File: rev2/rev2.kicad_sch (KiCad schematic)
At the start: 32 parts, among them J1 Termination, J2 CAN1, J3 Termination, J4 CAN2, J5 SWD ASYNC, J6 LIN Pots, J7 AIN, SW1 SW_Push, SW2 SW_SPDT, U1 STM32F429ZITx, U2 TJA1051T, U3 TJA1051T, U5 AMS1117-3.3, Y3 16MHz

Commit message: got the pcb into size constraint now need to try and see if routing is possible
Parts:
- added C30, C31, C32, C33, C38, C39, C40, C41, C42, C43, C44, C45, C46, C48: 100n, Capacitor_SMD:C_0603_1608Metric_Pad1.08x0.95mm_HandSolder, symbol Device:C
- added C47: 4.7u, Capacitor_SMD:C_0603_1608Metric_Pad1.08x0.95mm_HandSolder, symbol Device:C
- added C49: 1u, Capacitor_SMD:C_0603_1608Metric_Pad1.08x0.95mm_HandSolder, symbol Device:C
- added J10: GPIO, TerminalBlock_Phoenix:TerminalBlock_Phoenix_MPT-0,5-8-2.54_1x08_P2.54mm_Horizontal, symbol Connector:Screw_Terminal_01x08
- added J8: USB_OTG, Connector_USB:USB_Mini-B_Wuerth_65100516121_Horizontal, symbol Connector:USB_OTG
- added J9: PWR_USB, Connector_USB:USB_C_Receptacle_GCT_USB4105-xx-A_16P_TopMnt_Horizontal, symbol Connector:USB_C_Receptacle_PowerOnly_6P
- added U6: ~, Package_TO_SOT_SMD:SOT-23-5_HandSoldering, symbol custom parts library:STMPS2151STR
- C21, C22, C23, C24, C25, C28, C29: footprint (none) -> Capacitor_SMD:C_0603_1608Metric_Pad1.08x0.95mm_HandSolder
- C26: renamed from C24; footprint Capacitor_SMD:C_0603_1608Metric -> Capacitor_SMD:C_0603_1608Metric_Pad1.08x0.95mm_HandSolder
- C27: renamed from C25; footprint Capacitor_SMD:C_0603_1608Metric -> Capacitor_SMD:C_0603_1608Metric_Pad1.08x0.95mm_HandSolder
- J1, J3: footprint (none) -> Connector_PinHeader_2.54mm:PinHeader_1x02_P2.54mm_Vertical
- J2, J4: footprint (none) -> TerminalBlock_Phoenix:TerminalBlock_Phoenix_MPT-0,5-2-2.54_1x02_P2.54mm_Horizontal
- J5: footprint (none) -> Connector_PinHeader_2.54mm:PinHeader_2x05_P2.54mm_Vertical
- J6, J7: footprint (none) -> TerminalBlock_Phoenix:TerminalBlock_Phoenix_MPT-0,5-4-2.54_1x04_P2.54mm_Horizontal
- R1, R2, R4, R5, R6, R7, R8: footprint (none) -> Resistor_SMD:R_0603_1608Metric_Pad0.98x0.95mm_HandSolder
- R3: renamed from R2; value 47 -> 0; footprint Resistor_SMD:R_0603_1608Metric -> Resistor_SMD:R_0603_1608Metric_Pad0.98x0.95mm_HandSolder
- SW1: footprint (none) -> Button_Switch_SMD:SW_SPST_PTS645
- SW2: footprint (none) -> Button_Switch_SMD:SW_SPDT_CK-JS102011SAQN
- U4: footprint (none) -> Package_LGA:Bosch_LGA-14_3x2.5mm_P0.5mm
- renumbered Y3 to Y1
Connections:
- net +3.3V: now also C30.1, C31.1, C32.1, C33.1, C38.1, C39.1, C40.1, C41.1, C42.1, C43.1, C44.1, C45.1, C46.1, C47.1, C48.1, C49.1
- net +5V: now also J9.A9 (VBUS), J9.B9 (VBUS), U6.5 (VIN)
- net GND: now also C30.2, C31.2, C32.2, C33.2, C38.2, C39.2, C40.2, C41.2, C42.2, C43.2, C44.2, C45.2, C46.2, C47.2, C48.2, C49.2, J8.5 (GND), J8.6 (Shield), J9.A12 (GND), J9.B12 (GND), J9.S1 (SHIELD), U6.2 (GND)
- net GPIO7: now also U1.122 (PD6), J10.2 (Pin_2); no longer U1.123 (PD7)
- net GPIO8: now also U1.123 (PD7), J10.1 (Pin_1); no longer U1.77 (PD8)
- net Silent Mode 2: now also U1.77 (PD8); no longer U1.75 (PB14)
- net STMPS2151STR_EN: now reaches U1.1 (PE2)
- net STMPS2151STR_EN: now also U6.4 (EN)
- net STMPS2151STR_FAULT: now reaches U1.2 (PE3)
- net STMPS2151STR_FAULT: now also U6.3 (FAULT)
- net USB+: now reaches U1.76 (PB15)
- net USB+: now also J8.3 (D+)
- net CANH1+ renamed CAN1+
- net CANH2+ renamed CAN2+
- net CANL1- renamed CAN1-
- net CANL2- renamed CAN2-
- net GPIO1: no longer names the net of U1.129 (PG14)
- net GPIO1: now also J10.3 (Pin_3)
- net GPIO2: no longer names the net of U1.128 (PG13)
- net GPIO2: now also J10.4 (Pin_4)
- net GPIO3: no longer names the net of U1.127 (PG12)
- net GPIO3: now also J10.5 (Pin_5)
- net GPIO4: no longer names the net of U1.126 (PG11)
- net GPIO4: now also J10.6 (Pin_6)
- net GPIO5: no longer names the net of U1.125 (PG10)
- net GPIO5: now also J10.7 (Pin_7)
- net GPIO6: no longer names the net of U1.124 (PG9)
- net GPIO6: now also J10.8 (Pin_8)
- new net USB-: J8.2 (D-), U1.75 (PB14)
- new net VBUS1: J8.1 (VBUS), U6.1 (OUT)
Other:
- removed sheet Filtering
- note added: "Analog Filtering"
- note added: "VDD and Vbat Filtering"
- moved on the sheet: C25, C28, C29, J5, R2, R6, R7, R8, U5

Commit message: did like a quarter of the routing
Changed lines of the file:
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@@
     )
   )
-  (symbol (lib_id "Device:C") (at 160.02 250.19 0) (unit 1)
-    (in_bom yes) (on_board yes) (dnp no) (fields_autoplaced)
-    (property "Reference" "C21" (at 163.83 248.92 0)
+  (symbol (lib_id "Device:C") (at 160.02 250.19 0) (mirror y) (unit 1)
+    (in_bom yes) (on_board yes) (dnp no)
+    (property "Reference" "C21" (at 156.21 248.92 0)
       (effects (font (size 1.27 1.27)) (justify left))
     )
-    (property "Value" "2.2u" (at 163.83 251.46 0)
+    (property "Value" "2.2u" (at 156.21 251.46 0)
       (effects (font (size 1.27 1.27)) (justify left))
     )
-    (property "Footprint" "Capacitor_SMD:C_0603_1608Metric_Pad1.08x0.95mm_HandSolder" (at 160.9852 254 0)
+    (property "Footprint" "Capacitor_SMD:C_0603_1608Metric_Pad1.08x0.95mm_HandSolder" (at 159.0548 254 0)
       (effects (font (size 1.27 1.27)) hide)
     )

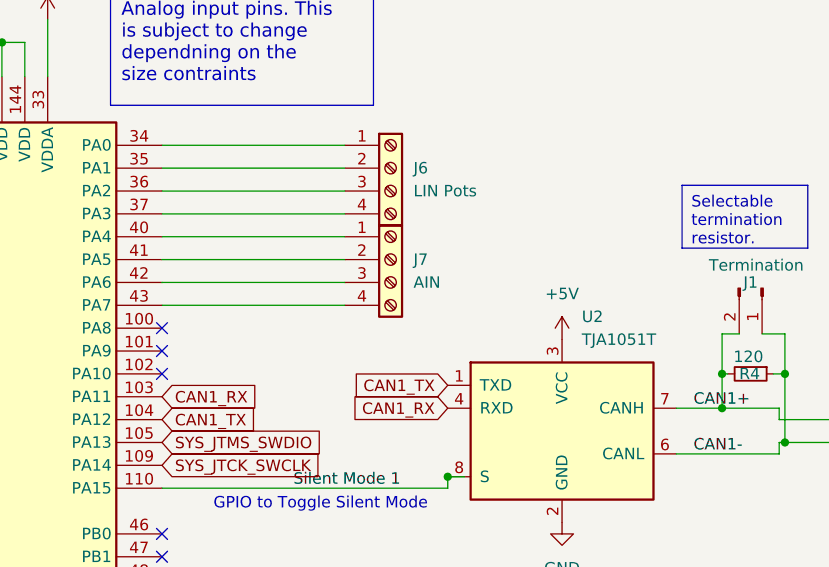
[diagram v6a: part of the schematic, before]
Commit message: finished the pcb routing except the usb C now I just need to do the DRC
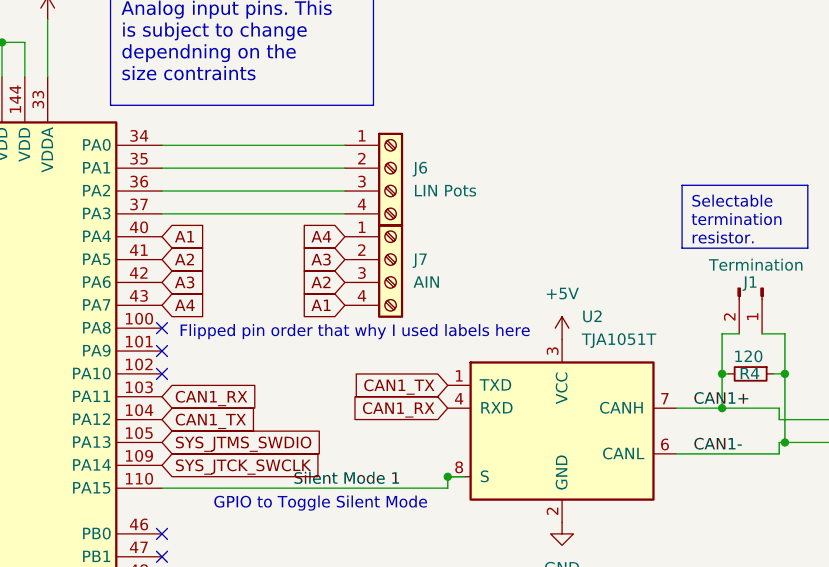
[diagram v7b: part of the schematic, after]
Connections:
- net A1: now reaches U1.40 (PA4)
- net A1: now also J7.4 (Pin_4); no longer J7.1 (Pin_1)
- net A2: now reaches U1.41 (PA5)
- net A2: now also J7.3 (Pin_3); no longer J7.2 (Pin_2)
- net A3: now reaches U1.42 (PA6)
- net A3: now also J7.2 (Pin_2); no longer J7.3 (Pin_3)
- net A4: now reaches U1.43 (PA7)
- net A4: now also J7.1 (Pin_1); no longer J7.4 (Pin_4)
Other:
- note added: "Flipped pin order that why I used labels here"
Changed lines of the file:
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@@
-    (stroke (width 0) (type default))
-  )
-  (wire (pts (xy 243.84 93.98) (xy 264.16 93.98))
     (stroke (width 0) (type default))
   )
@@
     (stroke (width 0) (type default))
   )
-  (wire (pts (xy 243.84 101.6) (xy 264.16 101.6))
-    (stroke (width 0) (type default))
-  )
   (wire (pts (xy 361.315 76.835) (xy 368.3 76.835))
     (stroke (width 0) (type default))
@@
     (stroke (width 0) (type default))
   )
-  (wire (pts (xy 243.84 96.52) (xy 264.16 96.52))
-    (stroke (width 0) (type default))
-  )
   (wire (pts (xy 286.385 34.925) (xy 286.385 38.735))
     (stroke (width 0) (type default))
@@
   )
   (wire (pts (xy 220.98 72.39) (xy 223.52 72.39))
-    (stroke (width 0) (type default))
-  )
-  (wire (pts (xy 243.84 99.06) (xy 264.16 99.06))
     (stroke (width 0) (type default))
   )
@@
     (effects (font (size 1.27 1.27)) (justify left bottom))
   )
+  (text "Flipped pin order that why I used labels here \n" (at 245.745 105.41 0)
+    (effects (font (size 1.27 1.27)) (justify left bottom))
+  )
   (text "GPIO to Toggle Silent Mode\n" (at 249.555 124.46 0)
     (effects (font (size 1.27 1.27)) (justify left bottom))
@@
     )
   )
+  (global_label "A4" (shape input) (at 264.16 93.98 180) (fields_autoplaced)
+    (effects (font (size 1.27 1.27)) (justify right))
+    (property "Intersheetrefs" "${INTERSHEET_REFS}" (at 258.8767 93.98 0)
+      (effects (font (size 1.27 1.27)) (justify right) hide)
+    )
+  )
   (global_label "USB-" (shape input) (at 243.84 162.56 0) (fields_autoplaced)
     (effects (font (size 1.27 1.27)) (justify left))
@@
     )
   )
+  (global_label "A1" (shape input) (at 243.84 93.98 0) (fields_autoplaced)
+    (effects (font (size 1.27 1.27)) (justify left))
+    (property "Intersheetrefs" "${INTERSHEET_REFS}" (at 249.1233 93.98 0)
+      (effects (font (size 1.27 1.27)) (justify left) hide)
+    )
+  )
   (global_label "CAN2_TX" (shape input) (at 243.84 160.02 0) (fields_autoplaced)
     (effects (font (size 1.27 1.27)) (justify left))
@@
     )
   )
+  (global_label "A2" (shape input) (at 264.16 99.06 180) (fields_autoplaced)
+    (effects (font (size 1.27 1.27)) (justify right))
+    (property "Intersheetrefs" "${INTERSHEET_REFS}" (at 258.8767 99.06 0)
+      (effects (font (size 1.27 1.27)) (justify right) hide)
+    )
+  )
+  (global_label "A1" (shape input) (at 264.16 101.6 180) (fields_autoplaced)
+    (effects (font (size 1.27 1.27)) (justify right))
+    (property "Intersheetrefs" "${INTERSHEET_REFS}" (at 258.8767 101.6 0)
+      (effects (font (size 1.27 1.27)) (justify right) hide)
+    )
+  )
   (global_label "CAN1_RX" (shape input) (at 275.59 113.03 180) (fields_autoplaced)
     (effects (font (size 1.27 1.27)) (justify right))
@@
     )
   )
+  (global_label "A3" (shape input) (at 243.84 99.06 0) (fields_autoplaced)
+    (effects (font (size 1.27 1.27)) (justify left))
+    (property "Intersheetrefs" "${INTERSHEET_REFS}" (at 249.1233 99.06 0)
+      (effects (font (size 1.27 1.27)) (justify left) hide)
+    )
+  )
   (global_label "GPIO8" (shape input) (at 243.84 231.14 0) (fields_autoplaced)
     (effects (font (size 1.27 1.27)) (justify left))
@@
     )
   )
+  (global_label "A3" (shape input) (at 264.16 96.52 180) (fields_autoplaced)
+    (effects (font (size 1.27 1.27)) (justify right))
+    (property "Intersheetrefs" "${INTERSHEET_REFS}" (at 258.8767 96.52 0)
+      (effects (font (size 1.27 1.27)) (justify right) hide)
+    )
+  )
+  (global_label "A2" (shape input) (at 243.84 96.52 0) (fields_autoplaced)
+    (effects (font (size 1.27 1.27)) (justify left))
+    (property "Intersheetrefs" "${INTERSHEET_REFS}" (at 249.1233 96.52 0)
+      (effects (font (size 1.27 1.27)) (justify left) hide)
+    )
+  )
   (global_label "USB+" (shape input) (at 126.365 205.105 0) (fields_autoplaced)
     (effects (font (size 1.27 1.27)) (justify left))
@@
     )
   )
+  (global_label "A4" (shape input) (at 243.84 101.6 0) (fields_autoplaced)
+    (effects (font (size 1.27 1.27)) (justify left))
+    (property "Intersheetrefs" "${INTERSHEET_REFS}" (at 249.1233 101.6 0)
+      (effects (font (size 1.27 1.27)) (justify left) hide)
+    )
+  )

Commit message: added finishing touches to the rev 2 design
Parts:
- SW2: footprint Button_Switch_SMD:SW_SPDT_CK-JS102011SAQN -> Button_Switch_SMD:SW_SPDT_PCM12
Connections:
- net GPIO7: now also J10.8 (Pin_8); no longer J10.2 (Pin_2)
- net GPIO8: now also J10.7 (Pin_7); no longer J10.1 (Pin_1)
- net GPIO4: now reaches J10.3 (Pin_3)
- net GPIO4: now also U1.127 (PG12); no longer U1.129 (PG14)
- net GPIO3: now reaches J10.4 (Pin_4)
- net GPIO3: now also U1.126 (PG11); no longer U1.128 (PG13)
- net GPIO2: now reaches J10.5 (Pin_5)
- net GPIO2: now also U1.125 (PG10); no longer U1.127 (PG12)
- net GPIO1: now reaches J10.6 (Pin_6)
- net GPIO1: now also U1.124 (PG9); no longer U1.126 (PG11)
- net linpot1: now reaches U1.34 (PA0)
- net linpot1: now also J6.4 (Pin_4); no longer J6.1 (Pin_1)
- net linpot2: now reaches U1.35 (PA1)
- net linpot2: now also J6.3 (Pin_3); no longer J6.2 (Pin_2)
- net linpot3: now reaches U1.36 (PA2)
- net linpot3: now also J6.2 (Pin_2); no longer J6.3 (Pin_3)
- net linpot4: now reaches U1.37 (PA3)
- net linpot4: now also J6.1 (Pin_1); no longer J6.4 (Pin_4)
- new net GPIO5: J10.2 (Pin_2), U1.128 (PG13)
- new net GPIO6: J10.1 (Pin_1), U1.129 (PG14)
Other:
- note added: "GPIO"
- moved on the sheet: J10
